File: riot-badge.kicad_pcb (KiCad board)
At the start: 4 copper layers, 99.1 x 99.1 mm, 418 parts, among them J1 SAO, J2 UEXT, J3 SWD, J4 3.5 mm "CAN" Connector, J5 USB_C_Receptacle_USB2.0_16P, J6 BAT, J8 uSD card, SW1 SW_Push, SW10 SW_Push, SW2 SW_Push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

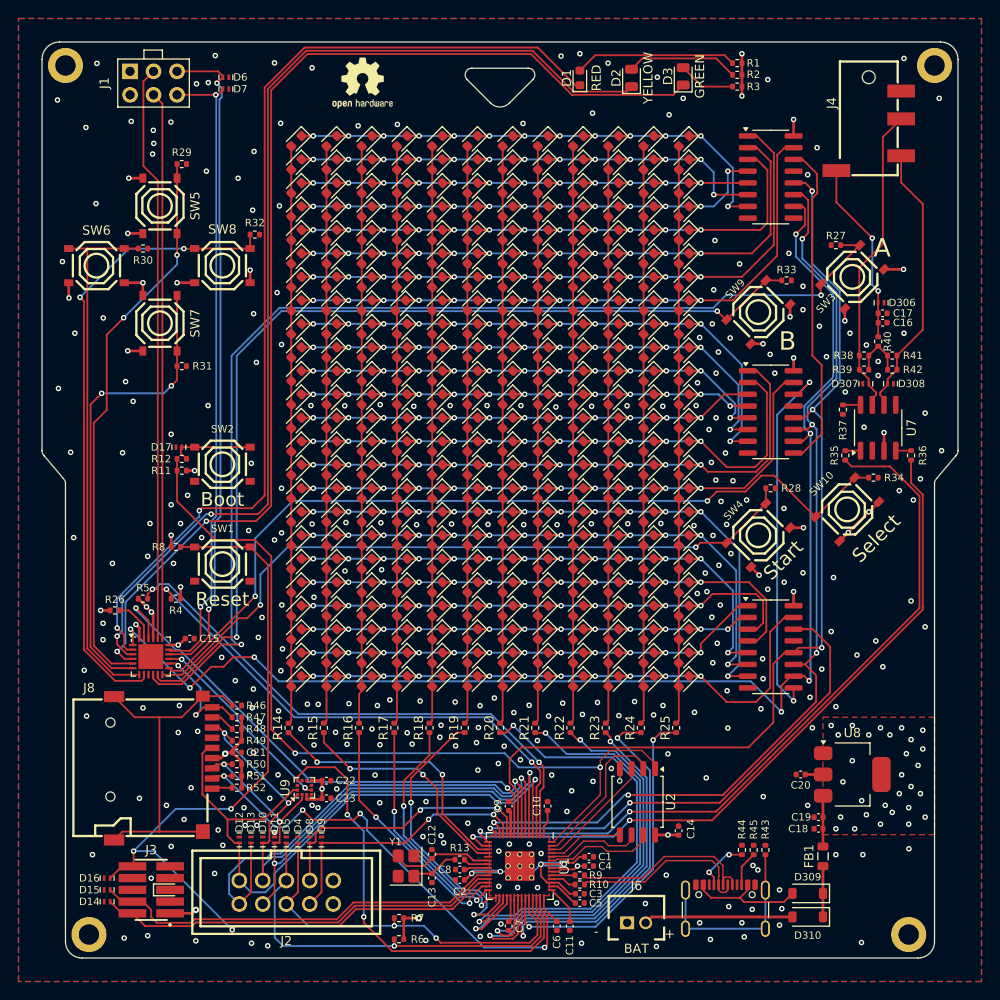
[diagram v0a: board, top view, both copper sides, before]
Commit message: PCB: Add draft silkscreen decoration
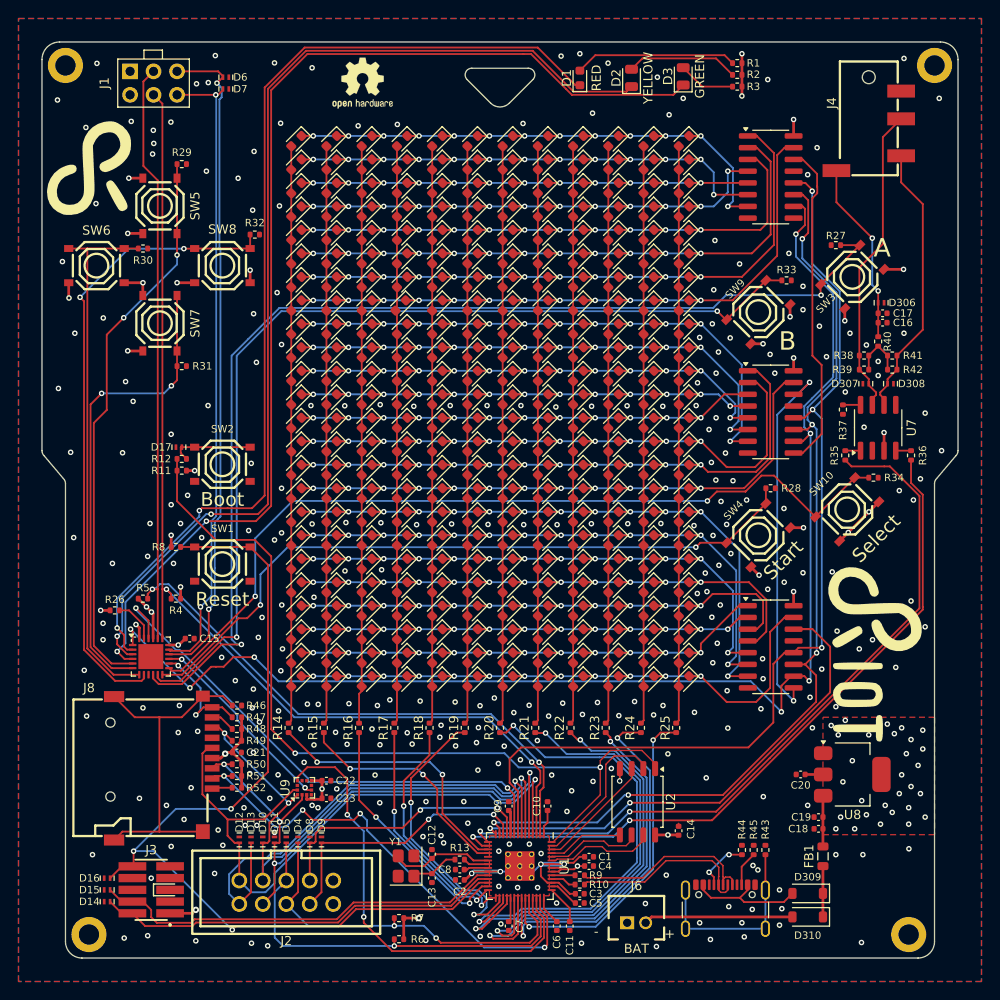
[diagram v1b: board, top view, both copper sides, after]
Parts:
- added G***: LOGO, custom:riot_logo_R, F.Cu at (35.4, 39.1)
- added G***: LOGO, custom:riot_logo_full_small, F.Cu at (115.5, 91.6)
- added G***: LOGO, custom:image_hacking_together, B.Cu at (74.5, 85.7)
- added G***: LOGO, custom:riot_logo_full, B.Cu at (75.0, 48.5)
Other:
- board text added: "Join the RIOT!"
